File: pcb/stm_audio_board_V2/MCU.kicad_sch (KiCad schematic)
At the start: 9 parts, among them SW1 SW_SPST, U3 STM32H747IGTx, Y2 X1E0000210132

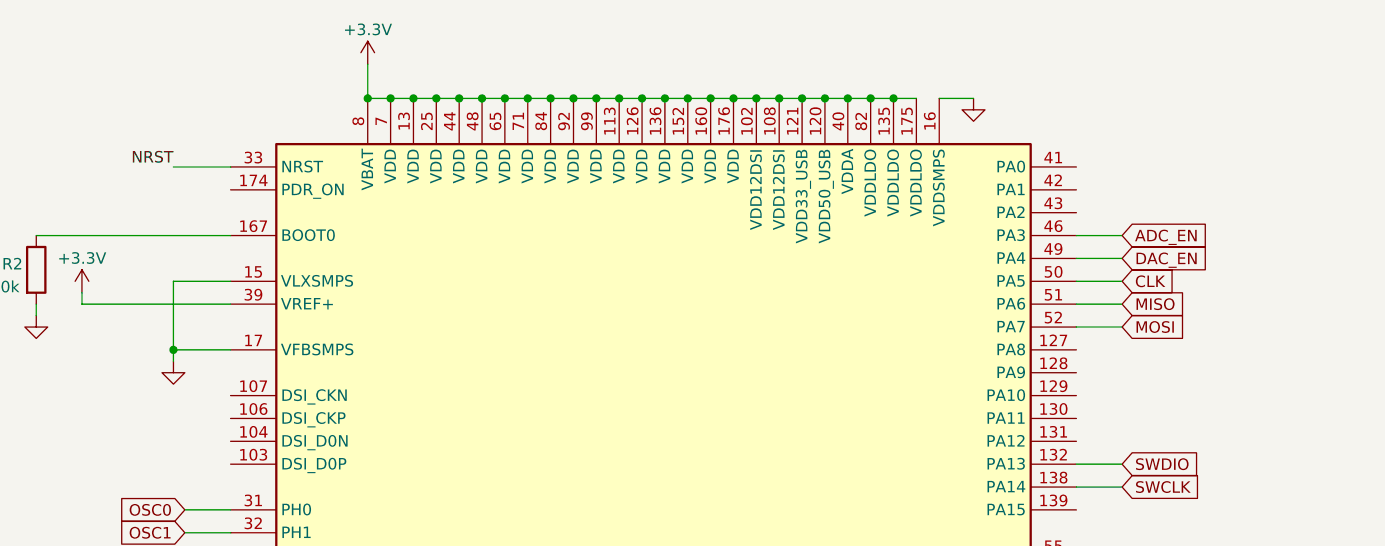
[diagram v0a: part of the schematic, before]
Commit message: Revert "smps setup is used"
This reverts commit c545ff16c6c59c28f3eb4762b27085b24475d59c.
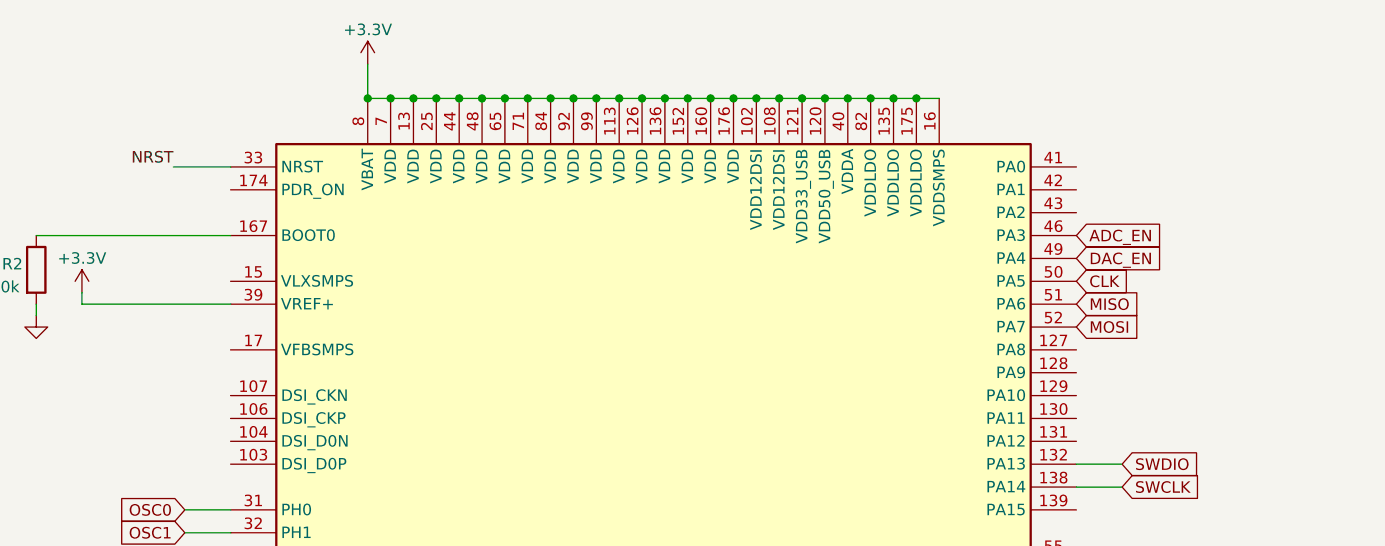
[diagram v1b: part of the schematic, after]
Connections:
- net +3.3V: now also U3.16 (VDDSMPS)
- net GND: no longer U3.15 (VLXSMPS), U3.16 (VDDSMPS), U3.17 (VFBSMPS)
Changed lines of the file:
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@@
   (junction (at 140.97 213.36) (diameter 0) (color 0 0 0 0)
   )
-  (junction (at 137.16 58.42) (diameter 0) (color 0 0 0 0)
-  )
   (junction (at 316.23 91.44) (diameter 0) (color 0 0 0 0)
   )
+  (junction (at 204.47 30.48) (diameter 0) (color 0 0 0 0)
+  )
+  (junction (at 140.97 215.9) (diameter 0) (color 0 0 0 0)
+  )
+  (junction (at 163.83 30.48) (diameter 0) (color 0 0 0 0)
+  )
   (junction (at 217.17 30.48) (diameter 0) (color 0 0 0 0)
   )
-  (junction (at 204.47 30.48) (diameter 0) (color 0 0 0 0)
-  )
-  (junction (at 140.97 215.9) (diameter 0) (color 0 0 0 0)
-  )
-  (junction (at 163.83 30.48) (diameter 0) (color 0 0 0 0)
-  )
   (junction (at 194.31 30.48) (diameter 0) (color 0 0 0 0)
   )
@@
   (junction (at 184.15 30.48) (diameter 0) (color 0 0 0 0)
   )
+  (junction (at 219.71 30.48) (diameter 0) (color 0 0 0 0)
+  )
   (junction (at 189.23 231.14) (diameter 0) (color 0 0 0 0)
   )
@@
     (stroke (width 0) (type default))
   )
+  (wire (pts (xy 217.17 30.48) (xy 219.71 30.48))
+    (stroke (width 0) (type default))
+  )
   (wire (pts (xy 189.23 30.48) (xy 191.77 30.48))
     (stroke (width 0) (type default))
@@
     (stroke (width 0) (type default))
   )
-  (wire (pts (xy 143.51 50.8) (xy 137.16 50.8))
-    (stroke (width 0) (type default))
-  )
   (wire (pts (xy 214.63 30.48) (xy 217.17 30.48))
     (stroke (width 0) (type default))
   )
+  (wire (pts (xy 219.71 30.48) (xy 222.25 30.48))
+    (stroke (width 0) (type default))
+  )
   (wire (pts (xy 191.77 30.48) (xy 194.31 30.48))
     (stroke (width 0) (type default))
@@
     (stroke (width 0) (type default))
   )
-  (wire (pts (xy 242.57 45.72) (xy 237.49 45.72))
-    (stroke (width 0) (type default))
-  )
   (wire (pts (xy 237.49 137.16) (xy 241.3 137.16))
     (stroke (width 0) (type default))
@@
     (stroke (width 0) (type default))
   )
-  (wire (pts (xy 137.16 58.42) (xy 137.16 59.69))
-    (stroke (width 0) (type default))
-  )
   (wire (pts (xy 186.69 231.14) (xy 189.23 231.14))
     (stroke (width 0) (type default))
@@
     (stroke (width 0) (type default))
   )
-  (wire (pts (xy 137.16 50.8) (xy 137.16 58.42))
-    (stroke (width 0) (type default))
-  )
   (wire (pts (xy 237.49 132.08) (xy 241.3 132.08))
     (stroke (width 0) (type default))
@@
     (stroke (width 0) (type default))
   )
-  (wire (pts (xy 242.57 53.34) (xy 237.49 53.34))
-    (stroke (width 0) (type default))
-  )
   (wire (pts (xy 140.97 218.44) (xy 140.97 215.9))
     (stroke (width 0) (type default))
   )
-  (wire (pts (xy 242.57 55.88) (xy 237.49 55.88))
-    (stroke (width 0) (type default))
-  )
   (wire (pts (xy 317.5 39.37) (xy 341.63 39.37))
     (stroke (width 0) (type default))
@@
     (stroke (width 0) (type default))
   )
-  (wire (pts (xy 242.57 48.26) (xy 237.49 48.26))
-    (stroke (width 0) (type default))
-  )
-  (wire (pts (xy 143.51 58.42) (xy 137.16 58.42))
-    (stroke (width 0) (type default))
-  )
   (wire (pts (xy 199.39 30.48) (xy 201.93 30.48))
     (stroke (width 0) (type default))
@@
     (stroke (width 0) (type default))
   )
-  (wire (pts (xy 222.25 30.48) (xy 226.06 30.48))
-    (stroke (width 0) (type default))
-  )
   (wire (pts (xy 237.49 139.7) (xy 241.3 139.7))
     (stroke (width 0) (type default))
@@
     (stroke (width 0) (type default))
   )
-  (wire (pts (xy 242.57 50.8) (xy 237.49 50.8))
-    (stroke (width 0) (type default))
-  )
   (wire (pts (xy 158.75 26.67) (xy 158.75 30.48))
     (stroke (width 0) (type default))
@@
   )
   (wire (pts (xy 132.08 220.98) (xy 143.51 220.98))
-    (stroke (width 0) (type default))
-  )
-  (wire (pts (xy 217.17 30.48) (xy 219.71 30.48))
     (stroke (width 0) (type default))
   )
@@
     )
   )
-  (global_label "MOSI" (shape input) (at 242.57 55.88 0) (fields_autoplaced)
-    (effects (font (size 1.27 1.27)) (justify left))
-    (property "Intersheetrefs" "${INTERSHEET_REFS}" (at 250.072 55.88 0)
-      (effects (font (size 1.27 1.27)) (justify left) hide)
-    )
-  )
-  (global_label "DAC_EN" (shape input) (at 242.57 48.26 0) (fields_autoplaced)
-    (effects (font (size 1.27 1.27)) (justify left))
-    (property "Intersheetrefs" "${INTERSHEET_REFS}" (at 252.5515 48.26 0)
+  (global_label "MOSI" (shape input) (at 237.49 55.88 0) (fields_autoplaced)
+    (effects (font (size 1.27 1.27)) (justify left))
+    (property "Intersheetrefs" "${INTERSHEET_REFS}" (at 244.992 55.88 0)
+      (effects (font (size 1.27 1.27)) (justify left) hide)
+    )
+  )
+  (global_label "DAC_EN" (shape input) (at 237.49 48.26 0) (fields_autoplaced)
+    (effects (font (size 1.27 1.27)) (justify left))
+    (property "Intersheetrefs" "${INTERSHEET_REFS}" (at 247.4715 48.26 0)
       (effects (font (size 1.27 1.27)) (justify left) hide)
     )
@@
     )
   )
-  (global_label "ADC_EN" (shape input) (at 242.57 45.72 0) (fields_autoplaced)
-    (effects (font (size 1.27 1.27)) (justify left))
-    (property "Intersheetrefs" "${INTERSHEET_REFS}" (at 252.5515 45.72 0)
+  (global_label "ADC_EN" (shape input) (at 237.49 45.72 0) (fields_autoplaced)
+    (effects (font (size 1.27 1.27)) (justify left))
+    (property "Intersheetrefs" "${INTERSHEET_REFS}" (at 247.4715 45.72 0)
       (effects (font (size 1.27 1.27)) (justify left) hide)
     )
@@
     )
   )
-  (global_label "MISO" (shape input) (at 242.57 53.34 0) (fields_autoplaced)
-    (effects (font (size 1.27 1.27)) (justify left))
-    (property "Intersheetrefs" "${INTERSHEET_REFS}" (at 250.072 53.34 0)
+  (global_label "MISO" (shape input) (at 237.49 53.34 0) (fields_autoplaced)
+    (effects (font (size 1.27 1.27)) (justify left))
+    (property "Intersheetrefs" "${INTERSHEET_REFS}" (at 244.992 53.34 0)
       (effects (font (size 1.27 1.27)) (justify left) hide)
     )
@@
     )
   )
-  (global_label "CLK" (shape input) (at 242.57 50.8 0) (fields_autoplaced)
-    (effects (font (size 1.27 1.27)) (justify left))
-    (property "Intersheetrefs" "${INTERSHEET_REFS}" (at 249.0439 50.8 0)
+  (global_label "CLK" (shape input) (at 237.49 50.8 0) (fields_autoplaced)
+    (effects (font (size 1.27 1.27)) (justify left))
+    (property "Intersheetrefs" "${INTERSHEET_REFS}" (at 243.9639 50.8 0)
       (effects (font (size 1.27 1.27)) (justify left) hide)
     )
@@
         )
       )
-    )
-  )
-  (symbol (lib_id "power:GND") (at 226.06 30.48 0) (unit 1)
-    (in_bom yes) (on_board yes) (dnp no) (fields_autoplaced)
-    (property "Reference" "#PWR010" (at 226.06 36.83 0)
-      (effects (font (size 1.27 1.27)) hide)
-    )
-    (property "Value" "GND" (at 226.06 35.56 0)
-      (effects (font (size 1.27 1.27)) hide)
-    )
-    (property "Footprint" "" (at 226.06 30.48 0)
-      (effects (font (size 1.27 1.27)) hide)
-    )
-    (property "Datasheet" "" (at 226.06 30.48 0)
-      (effects (font (size 1.27 1.27)) hide)
-    )
-    (pin "1")
-    (instances
-      (project "stm_audio_board_V2"
-        (path "/6997cf63-2615-4e49-9471-e7da1b6bae71"
-          (reference "#PWR010") (unit 1)
-        )
-        (path "/6997cf63-2615-4e49-9471-e7da1b6bae71/51aec99e-3301-49b6-8e7f-31ba63a05d64"
-          (reference "#PWR08") (unit 1)
-        )
-      )
-    )
-  )
-  (symbol (lib_id "power:GND") (at 137.16 59.69 0) (unit 1)
-    (in_bom yes) (on_board yes) (dnp no) (fields_autoplaced)
-    (property "Reference" "#PWR010" (at 137.16 66.04 0)
-      (effects (font (size 1.27 1.27)) hide)
-    )
-    (property "Value" "GND" (at 137.16 64.77 0)
-      (effects (font (size 1.27 1.27)) hide)
-    )
-    (property "Footprint" "" (at 137.16 59.69 0)
-      (effects (font (size 1.27 1.27)) hide)
-    )
-    (property "Datasheet" "" (at 137.16 59.69 0)
-      (effects (font (size 1.27 1.27)) hide)
-    )
-    (pin "1")
-    (instances
-      (project "stm_audio_board_V2"
-        (path "/6997cf63-2615-4e49-9471-e7da1b6bae71"
-          (reference "#PWR010") (unit 1)
-        )
-        (path "/6997cf63-2615-4e49-9471-e7da1b6bae71/51aec99e-3301-49b6-8e7f-31ba63a05d64"
-          (reference "#PWR06") (unit 1)
-        )
-      )

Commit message: smps setup is used
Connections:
- net +3.3V: no longer U3.16 (VDDSMPS)
- net GND: now also U3.15 (VLXSMPS), U3.16 (VDDSMPS), U3.17 (VFBSMPS)
